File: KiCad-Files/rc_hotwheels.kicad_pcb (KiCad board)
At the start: 2 copper layers, 29.5 x 21.6 mm, 16 parts, among them IC1 BD6211F-E2, IC2 MIC5504-3.3YM5-TR, M1 Motor_Connection, U1 STM32F070F6P6, U3 NRF24L01_Breakout

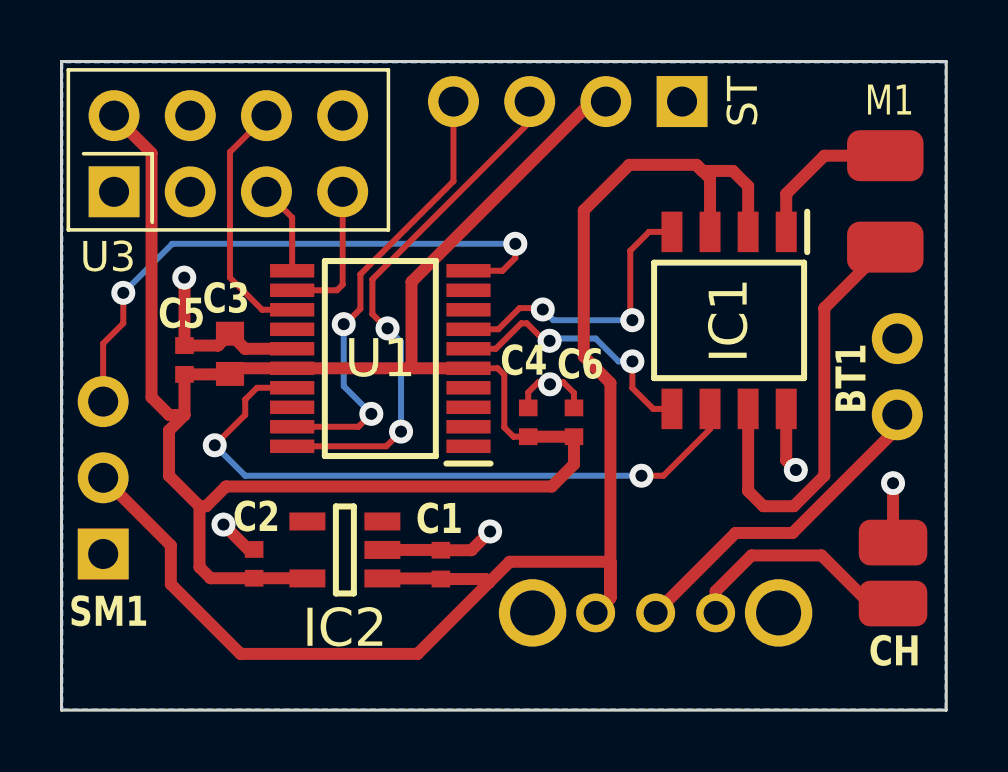
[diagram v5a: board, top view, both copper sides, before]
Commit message: PCB V2.2
-Updated Capacitors footprint
-Added reset pin for the MCU.
-PCB design improved

Co-Authored-By: Yazid Almazroua <98489302+yazidta@users.noreply.github.com>
Co-Authored-By: Soplica52 <100694324+Soplica52@users.noreply.github.com>
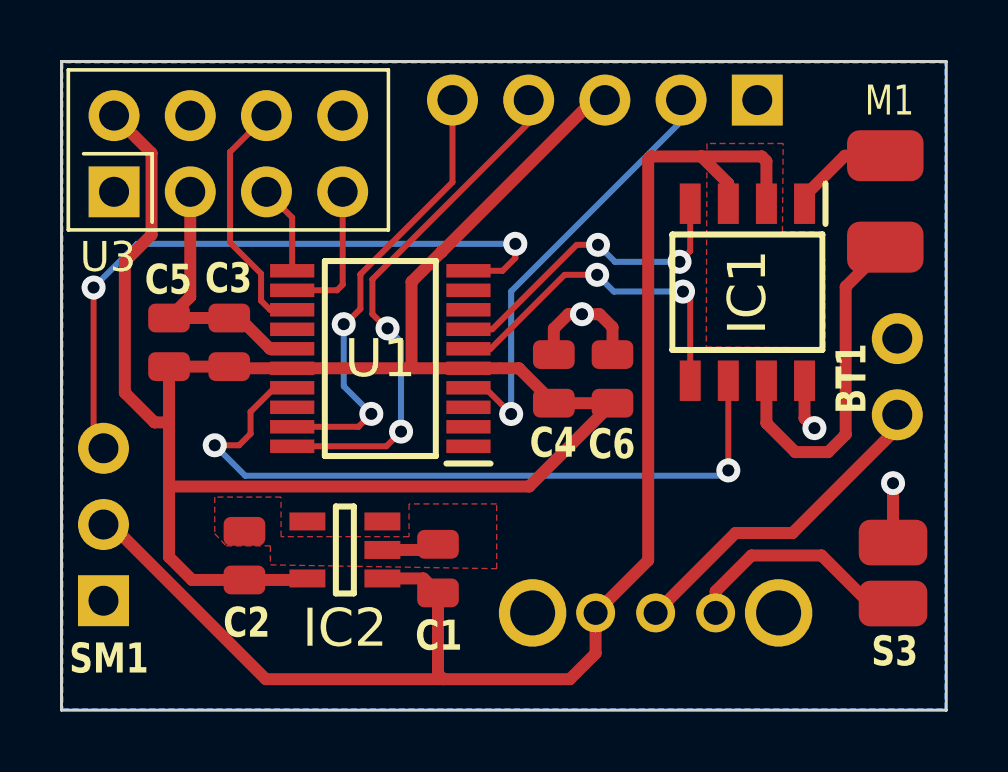
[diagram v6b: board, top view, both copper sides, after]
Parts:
- C1, C2, C4: footprint C1uF:CAPC1005X55N -> C1uF:CAPC2012X135N
- C3: footprint C4.7uF:CAPC1608X87N -> C1uF:CAPC2012X135N
- C5: footprint C100nF:CAPC1005X55N -> C1uF:CAPC2012X135N
- C6: footprint C10nF:CAPC1005X55N -> C1uF:CAPC2012X135N
- moved ST 2.51 mm to (83.6, 35.2)
- moved C6 1.93 mm to (76.8, 44.5), turned to 90 degrees
- moved C4 1.68 mm to (74.8, 44.5)
- moved SM1 1.56 mm to (59.8, 55.0)
- moved IC1 1.12 mm to (81.3, 41.6)
- moved C5 0.78 mm to (62.0, 43.3), turned to 90 degrees
- moved C2 0.42 mm to (64.5, 50.4)
- moved C3 0.38 mm to (64.0, 43.3), turned to 90 degrees
- moved C1 0.16 mm to (70.9, 50.8)
- renumbered CH to S3
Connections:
- C1 pad 1: GND -> Net-(IC2-GND)
- C2 pad 1: GND -> Net-(C2-Pad1)
- C3 pad 1: GND -> VR_OUT
- C3 pad 2: VR_OUT -> GND
- C5 pad 1: GND -> VR_OUT
- C5 pad 2: VR_OUT -> GND
- C6 pad 1: GND -> VR_OUT
- C6 pad 2: VR_OUT -> GND
- IC2 pad 2: GND -> Net-(IC2-GND)
- ST pad 2: VR_OUT -> RST
- ST pad 3: SYS_SWCLK -> VR_OUT
- ST pad 4: SYS_SWDIO -> SYS_SWCLK
- U1 pad 15: GND -> Net-(U1B-VSS)
- U1 pad 4: unconnected-(U1A-NRST-Pad4) -> RST
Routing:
- net RST: track 0.00 -> 14.9 mm, vias 0 -> 1
- net VR_OUT: track 62.9 -> 66.3 mm
- net Motor -: track 14.4 -> 11.5 mm
- net Motor Reverse: track 8.90 -> 11.5 mm
- net PWM: track 19.9 -> 22.4 mm
- net Motor Speed: track 21.9 -> 24.4 mm
- net VCC: track 50.6 -> 48.5 mm
- net Net-(IC2-GND): track 0.00 -> 1.93 mm
- net Motor +: track 5.10 -> 3.50 mm
- net GND: track 18.4 -> 16.9 mm, vias 6 -> 3
- net Motor Forward: track 9.92 -> 10.5 mm
- added copper zone on F.Cu, net Net-(C2-Pad1)
- added copper zone on B.Cu, net Net-(SM1--)
- added copper zone on F.Cu, net VCC
- removed copper zone on B.Cu, net GND

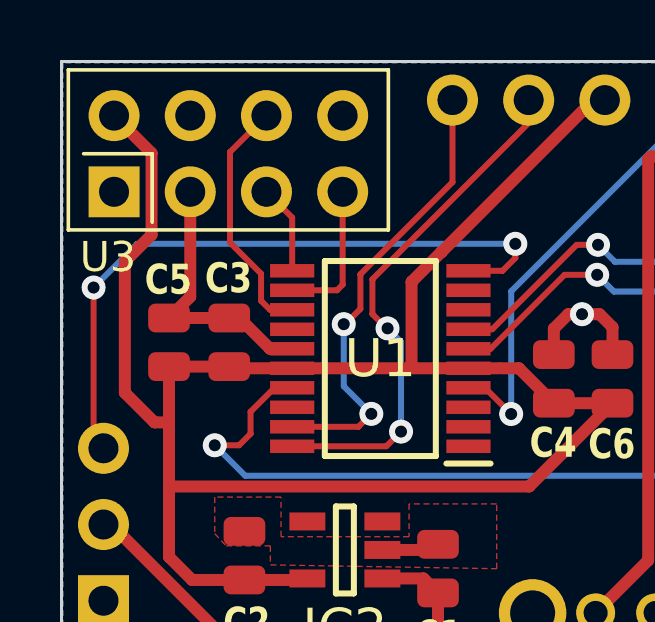
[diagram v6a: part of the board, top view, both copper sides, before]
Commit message: Fixed GNDS not connected.
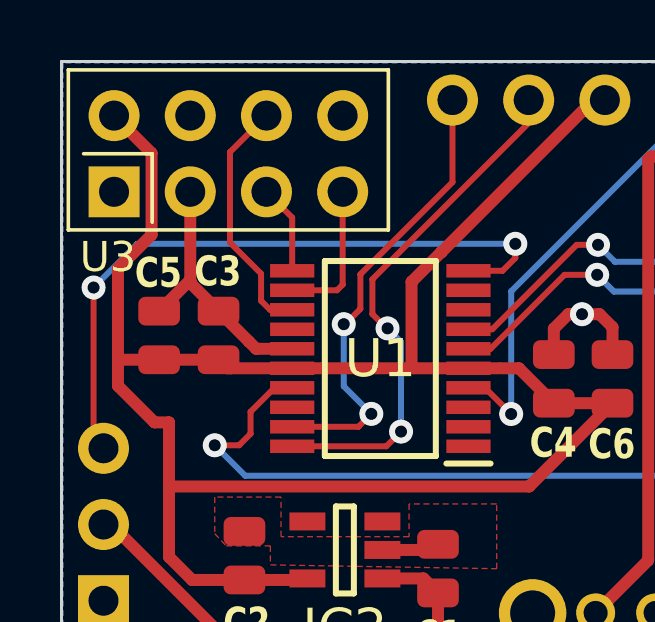
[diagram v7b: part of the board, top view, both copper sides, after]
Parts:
- moved C3 0.42 mm to (63.6, 43.1)
- moved C5 0.40 mm to (61.6, 43.1)
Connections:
- C1 pad 1: Net-(IC2-GND) -> GND
- C2 pad 1: Net-(C2-Pad1) -> GND
- IC2 pad 2: Net-(IC2-GND) -> GND
- U1 pad 15: Net-(U1B-VSS) -> GND
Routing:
- net Net-(IC2-GND): track 1.93 -> 0.00 mm
- net GND: track 16.9 -> 18.6 mm
- added copper zone on B.Cu, net GND
- removed copper zone on B.Cu, net Net-(SM1--)

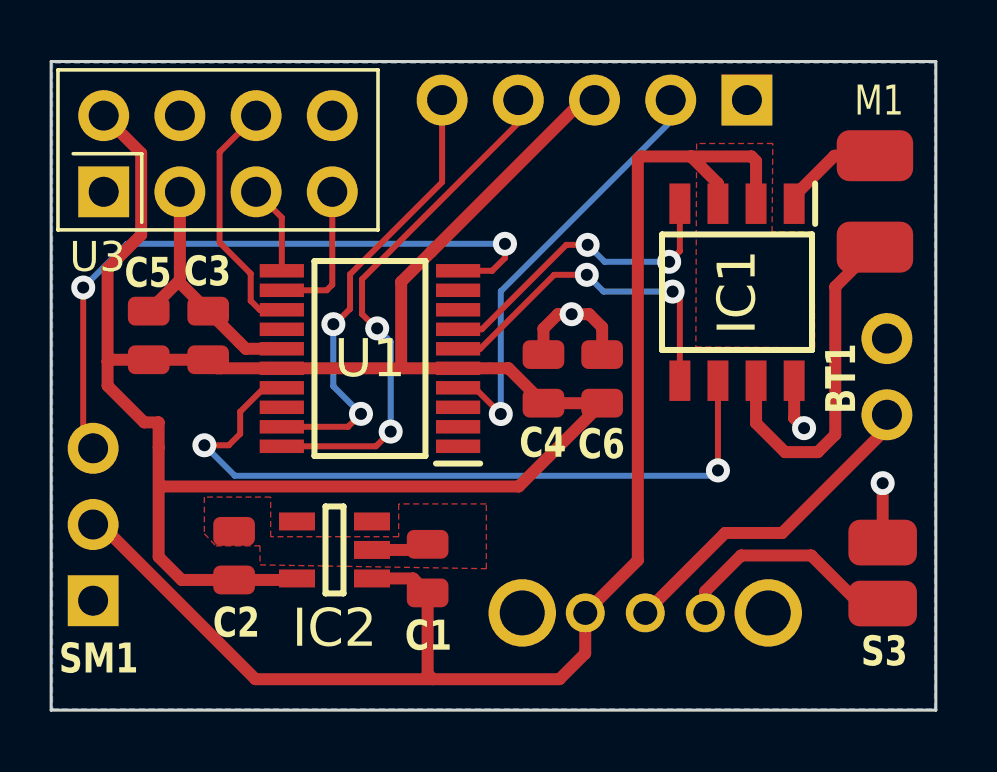
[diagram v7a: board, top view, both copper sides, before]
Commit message: PCB Update
Fixed all errors & warnings
Made the thermal reliefs bigger
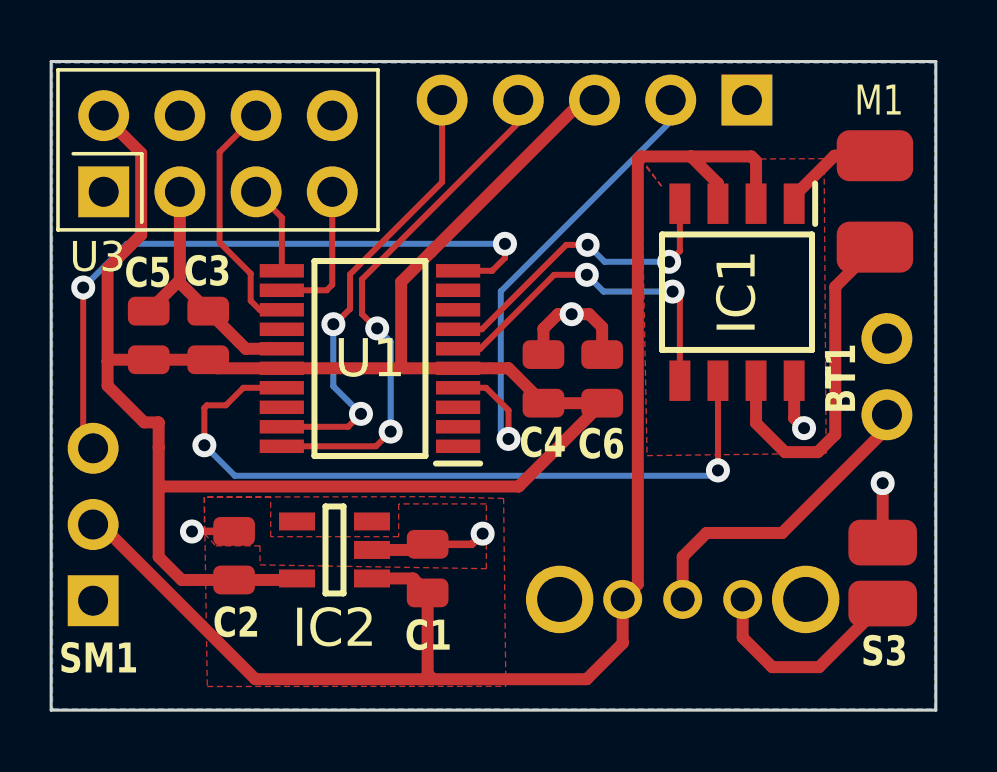
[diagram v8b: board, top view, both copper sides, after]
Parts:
- moved S1 1.33 mm to (79.4, 51.9)
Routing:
- net GND: track 18.6 -> 21.9 mm, vias 3 -> 5
- net RST: track 14.9 -> 16.7 mm
- net Net-(BT1-+): track 11.1 -> 10.5 mm
- net Net-(S3-BATT+): track 7.79 -> 7.22 mm
- net VCC: track 48.5 -> 49.0 mm
- added copper zone on F.Cu, net GND
